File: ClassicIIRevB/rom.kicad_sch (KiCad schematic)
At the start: 11 parts, among them J13 PROM select, U22 27C322, U23 27C322

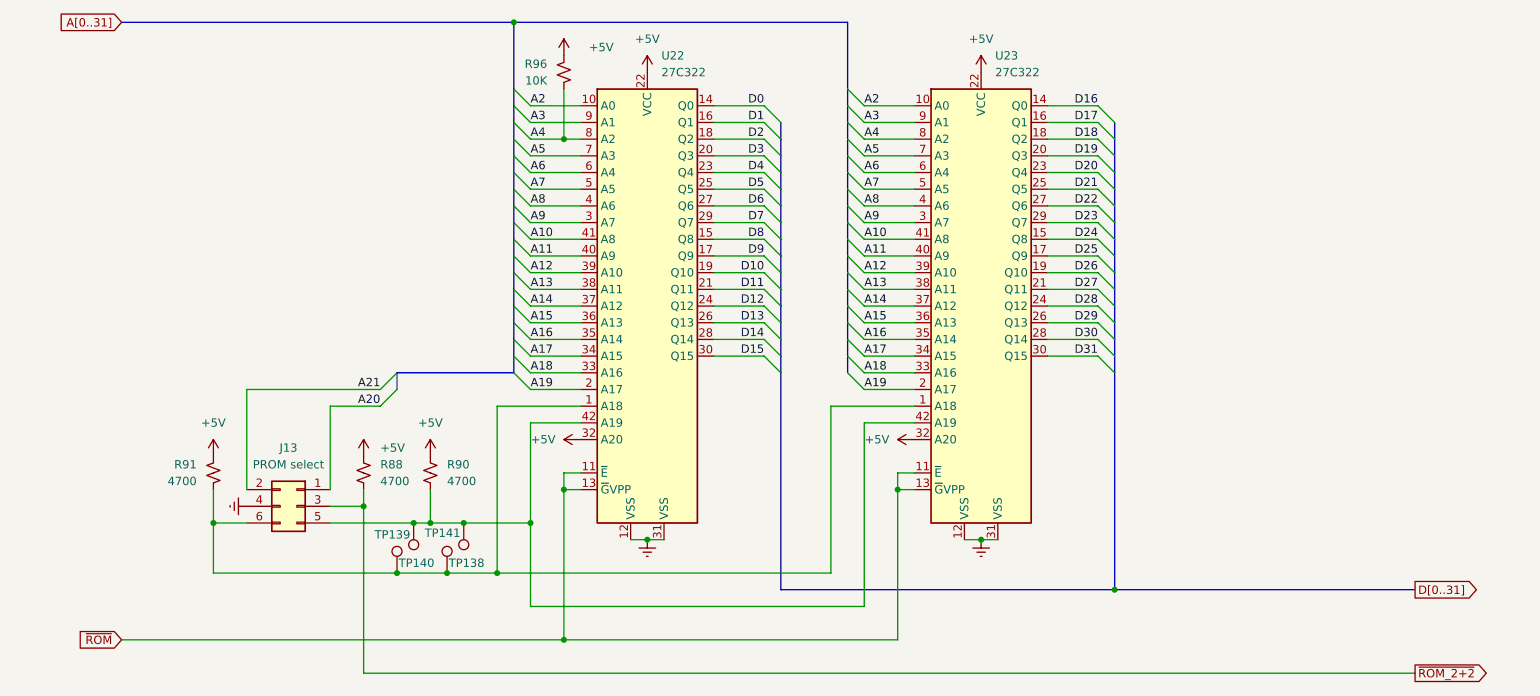
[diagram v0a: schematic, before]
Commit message: Show smaller ROM footprints
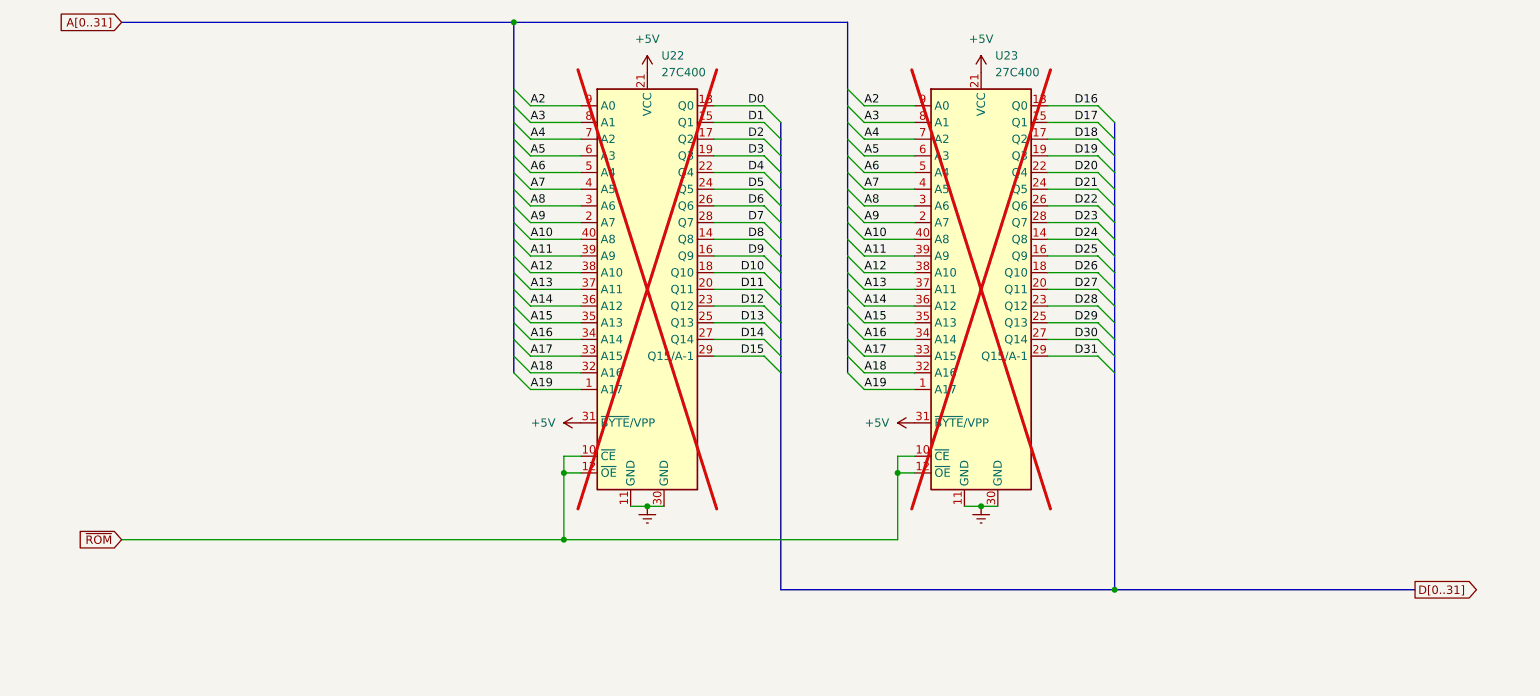
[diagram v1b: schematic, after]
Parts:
- removed J13: PROM select, Connector_PinHeader_2.54mm:PinHeader_2x03_P2.54mm_Vertical, symbol Connector_Generic:Conn_02x03_Odd_Even
- removed R88, R90, R91: 4700, MyPackage:SMD_0805_2012Metric_Pad1.25x1.65mm, symbol Device:R_Small_US
- removed R96: 10K, MyPackage:SMD_0805_2012Metric_Pad1.25x1.65mm, symbol Device:R_Small_US
- removed TP138, TP139, TP140, TP141: ~, MyPackage:TestPoint_THTPad_D1.0mm_Drill0.5mm, symbol Connector:TestPoint
- removed U22, U23: 27C322, Package_DIP:DIP-42_W15.24mm_Socket, symbol MyEprom:27C322
- added U22, U23: 27C400, MyPackage:DIP-40_W15.24mm_Socket_SmallPads, symbol MyEprom:27C400
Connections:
- net +5V: now also U22.21 (VCC), U22.31 (~{BYTE}/VPP), U23.21 (VCC), U23.31 (~{BYTE}/VPP)
- net A10: now also U22.40 (A8), U23.40 (A8)
- net A11: now also U22.39 (A9), U23.39 (A9)
- net A12: now also U22.38 (A10), U23.38 (A10)
- net A13: now also U22.37 (A11), U23.37 (A11)
- net A14: now also U22.36 (A12), U23.36 (A12)
- net A15: now also U22.35 (A13), U23.35 (A13)
- net A16: now also U22.34 (A14), U23.34 (A14)
- net A17: now also U22.33 (A15), U23.33 (A15)
- net A18: now also U22.32 (A16), U23.32 (A16)
- net A19: now also U22.1 (A17), U23.1 (A17)
- net A2: now also U22.9 (A0), U23.9 (A0)
- net A3: now also U22.8 (A1), U23.8 (A1)
- net A4: now also U22.7 (A2), U23.7 (A2)
- net A5: now also U22.6 (A3), U23.6 (A3)
- net A6: now also U22.5 (A4), U23.5 (A4)
- net A7: now also U22.4 (A5), U23.4 (A5)
- net A8: now also U22.3 (A6), U23.3 (A6)
- net A9: now also U22.2 (A7), U23.2 (A7)
- net D0: now also U22.13 (Q0)
- net D1: now also U22.15 (Q1)
- net D10: now also U22.18 (Q10)
- net D11: now also U22.20 (Q11)
- net D12: now also U22.23 (Q12)
- net D13: now also U22.25 (Q13)
- net D14: now also U22.27 (Q14)
- net D15: now also U22.29 (Q15/A-1)
- net D16: now also U23.13 (Q0)
- net D17: now also U23.15 (Q1)
- net D18: now also U23.17 (Q2)
- net D19: now also U23.19 (Q3)
- net D2: now also U22.17 (Q2)
- net D20: now also U23.22 (Q4)
- net D21: now also U23.24 (Q5)
- net D22: now also U23.26 (Q6)
- net D23: now also U23.28 (Q7)
- net D24: now also U23.14 (Q8)
- net D25: now also U23.16 (Q9)
- net D26: now also U23.18 (Q10)
- net D27: now also U23.20 (Q11)
- net D28: now also U23.23 (Q12)
- net D29: now also U23.25 (Q13)
- net D3: now also U22.19 (Q3)
- net D30: now also U23.27 (Q14)
- net D31: now also U23.29 (Q15/A-1)
- net D4: now also U22.22 (Q4)
- net D5: now also U22.24 (Q5)
- net D6: now also U22.26 (Q6)
- net D7: now also U22.28 (Q7)
- net D8: now also U22.14 (Q8)
- net D9: now also U22.16 (Q9)
- net GND: now also U22.11 (GND), U22.30 (GND), U23.11 (GND), U23.30 (GND)
- net ~{ROM}: now also U22.10 (~{CE}), U22.12 (~{OE}), U23.10 (~{CE}), U23.12 (~{OE})

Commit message: Switch to some "official" net names
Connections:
- net ~{ROM} renamed ~{ROM_SEL}

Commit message: update exports
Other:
- title: Macintosh Classic II Revision B -> Macintosh Classic II (Later Revision)
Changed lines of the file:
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@@
 	(paper "USLetter")
 	(title_block
-		(title "Macintosh Classic II Revision B")
-		(date "2025-06-04")
+		(title "Macintosh Classic II (Later Revision)")
+		(date "2025-06-16")
 		(company "Apple Computer")
 		(comment 1 "drawn by Bradley Bell")

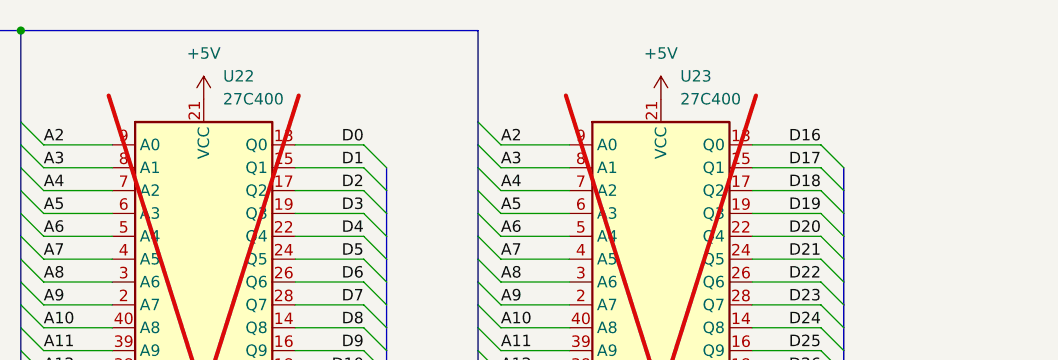
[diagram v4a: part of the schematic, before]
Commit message: Corrections to SMDs, more improved footprints
The later revision board reproduction design is now complete.
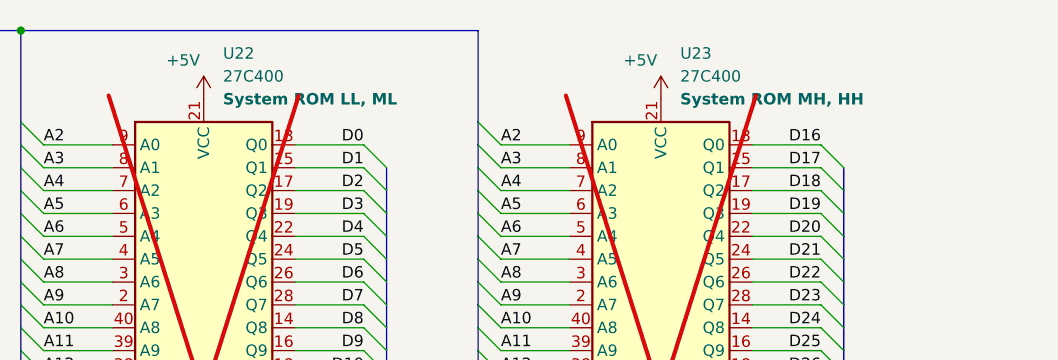
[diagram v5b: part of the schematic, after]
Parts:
- U22, U23: footprint MyPackage:DIP-40_W15.24mm_Socket_SmallPads -> MyPackage:DIP-40_W15.24mm_Socket
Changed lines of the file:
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@@
 	(title_block
 		(title "Macintosh Classic II (Later Revision)")
-		(date "2025-06-16")
+		(date "2025-06-21")
 		(company "Apple Computer")
 		(comment 1 "drawn by Bradley Bell")
@@
 		(on_board yes)
 		(dnp no)
-		(fields_autoplaced yes)
 		(property "Reference" "#PWR0231"
 			(at 175.26 64.77 0)
@@
 		)
 		(property "Value" "+5V"
-			(at 175.26 55.88 0)
+			(at 172.974 56.642 0)
 			(effects
 				(font
@@
 		(on_board yes)
 		(dnp no)
-		(fields_autoplaced yes)
 		(property "Reference" "#PWR0230"
 			(at 124.46 64.77 0)
@@
 		)
 		(property "Value" "+5V"
-			(at 124.46 55.88 0)
+			(at 122.174 56.642 0)
 			(effects
 				(font
@@
 		(fields_autoplaced yes)
 		(property "Reference" "U23"
-			(at 177.4033 58.42 0)
+			(at 177.4033 55.88 0)
 			(effects
 				(font
@@
 		)
 		(property "Value" "27C400"
-			(at 177.4033 60.96 0)
+			(at 177.4033 58.42 0)
 			(effects
 				(font
@@
 			)
 		)
-		(property "Footprint" "MyPackage:DIP-40_W15.24mm_Socket_SmallPads"
+		(property "Footprint" "MyPackage:DIP-40_W15.24mm_Socket"
 			(at 175.26 93.98 0)
 			(effects
@@
 			)
 		)
-		(property "Description" "OTP EPROM 4 Megabit (256K x 16 or 512K x 8)"
-			(at 175.26 93.98 0)
+		(property "Description" "System ROM MH, HH"
+			(at 177.4033 60.96 0)
 			(effects
 				(font
 					(size 1.27 1.27)
+					(thickness 0.254)
+					(bold yes)
 				)
-				(hide yes)
+				(justify left)
 			)
 		)
@@
 		(fields_autoplaced yes)
 		(property "Reference" "U22"
-			(at 126.6033 58.42 0)
+			(at 126.6033 55.88 0)
 			(effects
 				(font
@@
 		)
 		(property "Value" "27C400"
-			(at 126.6033 60.96 0)
+			(at 126.6033 58.42 0)
 			(effects
 				(font
@@
 			)
 		)
-		(property "Footprint" "MyPackage:DIP-40_W15.24mm_Socket_SmallPads"
+		(property "Footprint" "MyPackage:DIP-40_W15.24mm_Socket"
 			(at 124.46 93.98 0)
 			(effects
@@
 			)
 		)
-		(property "Description" "OTP EPROM 4 Megabit (256K x 16 or 512K x 8)"
-			(at 124.46 93.98 0)
+		(property "Description" "System ROM LL, ML"
+			(at 126.6033 60.96 0)
 			(effects
 				(font
 					(size 1.27 1.27)
+					(thickness 0.254)
+					(bold yes)
 				)
-				(hide yes)
+				(justify left)
 			)
 		)
